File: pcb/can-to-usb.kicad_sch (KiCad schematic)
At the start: 25 parts, among them J11 Programming connector, Q5 AO3401A, Q6 AO3401A, Q7 AO3400A, Q8 AO3400A, U13 STM32G431CBU6, U14 TJA1044GTK_3Z

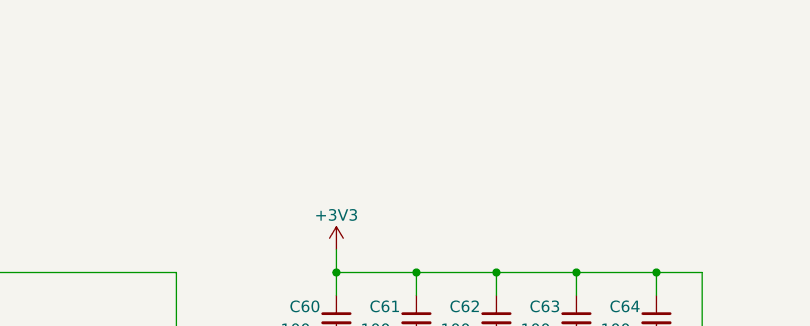
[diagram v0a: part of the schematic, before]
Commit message: [#5] Refactor the schematic
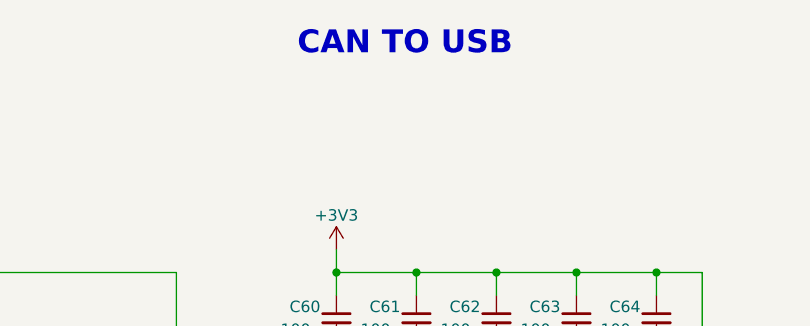
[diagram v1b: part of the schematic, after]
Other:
- note added: "CAN TO USB"
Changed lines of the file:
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@@
+		)
+	)
+	(text "CAN TO USB"
+		(exclude_from_sim no)
+		(at 137.16 33.02 0)
+		(effects
+			(font
+				(size 2.54 2.54)
+				(bold yes)
+			)
 		)
 	)
